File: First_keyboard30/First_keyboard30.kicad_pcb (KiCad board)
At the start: 2 copper layers, 238.1 x 57.2 mm, 0 parts

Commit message: circuit diagram compleat
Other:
- outline, holes or cut-outs redrawn

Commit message: pcb update
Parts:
- added D1: DIODE, kbd:D3_TH_SMD, F.Cu at (47.1, 93.0)
- added D10: DIODE, kbd:D3_TH_SMD, F.Cu at (218.6, 93.1)
- added D11: DIODE, kbd:D3_TH_SMD, F.Cu at (237.6, 93.1)
- added D12: DIODE, kbd:D3_TH_SMD, F.Cu at (261.4, 93.0)
- added D13: DIODE, kbd:D3_TH_SMD, F.Cu at (47.1, 110.7)
- added D14: DIODE, kbd:D3_TH_SMD, F.Cu at (66.2, 111.1)
- added D15: DIODE, kbd:D3_TH_SMD, F.Cu at (85.2, 111.0)
- added D16: DIODE, kbd:D3_TH_SMD, F.Cu at (104.2, 111.0)
- added D17: DIODE, kbd:D3_TH_SMD, F.Cu at (123.3, 111.0)
- added D18: DIODE, kbd:D3_TH_SMD, F.Cu at (142.4, 111.0)
- added D19: DIODE, kbd:D3_TH_SMD, F.Cu at (161.5, 110.3)
- added D2: DIODE, kbd:D3_TH_SMD, F.Cu at (66.2, 93.0)
- added D20: DIODE, kbd:D3_TH_SMD, F.Cu at (180.5, 110.4)
- added D21: DIODE, kbd:D3_TH_SMD, F.Cu at (199.5, 110.4)
- added D22: DIODE, kbd:D3_TH_SMD, F.Cu at (218.6, 110.3)
- added D23: DIODE, kbd:D3_TH_SMD, F.Cu at (237.5, 110.3)
- added D24: DIODE, kbd:D3_TH_SMD, F.Cu at (47.1, 129.3)
- added D25: DIODE, kbd:D3_TH_SMD, F.Cu at (66.2, 129.4)
- added D26: DIODE, kbd:D3_TH_SMD, F.Cu at (85.2, 129.4)
- added D27: DIODE, kbd:D3_TH_SMD, F.Cu at (104.2, 129.2)
- added D28: DIODE, kbd:D3_TH_SMD, F.Cu at (123.3, 129.2)
- added D29: DIODE, kbd:D3_TH_SMD, F.Cu at (142.3, 129.2)
- added D3: DIODE, kbd:D3_TH_SMD, F.Cu at (85.2, 93.0)
- added D30: DIODE, kbd:D3_TH_SMD, F.Cu at (243.4, 131.4)
- added D31: DIODE, kbd:D3_TH_SMD, F.Cu at (161.6, 129.3)
- added D32: DIODE, kbd:D3_TH_SMD, F.Cu at (180.5, 129.3)
- added D33: DIODE, kbd:D3_TH_SMD, F.Cu at (205.5, 129.3)
- added D34: DIODE, kbd:D3_TH_SMD, F.Cu at (243.4, 119.3)
- added D4: DIODE, kbd:D3_TH_SMD, F.Cu at (104.3, 92.9)
- added D5: DIODE, kbd:D3_TH_SMD, F.Cu at (123.3, 92.9)
- added D6: DIODE, kbd:D3_TH_SMD, F.Cu at (142.3, 93.0)
- added D7: DIODE, kbd:D3_TH_SMD, F.Cu at (161.5, 93.1)
- added D8: DIODE, kbd:D3_TH_SMD, F.Cu at (180.5, 93.1)
- added D9: DIODE, kbd:D3_TH_SMD, F.Cu at (199.5, 93.1)
- added SW1: RESET_SW, kbd:ResetSW, F.Cu at (32.9, 98.0)
- added SW10: KEY_SW, kbd:CherryMX_1u, F.Cu at (190.0, 92.5)
- added SW11: KEY_SW, kbd:CherryMX_1u, F.Cu at (209.0, 92.5)
- added SW12: KEY_SW, kbd:CherryMX_1u, F.Cu at (228.1, 92.5)
- added SW13: KEY_SW, kbd:CherryMX_1u, F.Cu at (251.9, 92.5)
- added SW14: KEY_SW, kbd:CherryMX_1u, F.Cu at (37.6, 111.6)
- added SW15: KEY_SW, kbd:CherryMX_1u, F.Cu at (56.6, 111.6)
- added SW16: KEY_SW, kbd:CherryMX_1u, F.Cu at (75.7, 111.6)
- added SW17: KEY_SW, kbd:CherryMX_1u, F.Cu at (94.7, 111.6)
- added SW18: KEY_SW, kbd:CherryMX_1u, F.Cu at (113.8, 111.6)
- added SW19: KEY_SW, kbd:CherryMX_1u, F.Cu at (132.8, 111.6)
- added SW2: KEY_SW, kbd:CherryMX_1u, F.Cu at (37.6, 92.5)
- added SW20: KEY_SW, kbd:CherryMX_1u, F.Cu at (151.9, 111.6)
- added SW21: KEY_SW, kbd:CherryMX_1u, F.Cu at (170.9, 111.6)
- added SW22: KEY_SW, kbd:CherryMX_1u, F.Cu at (190.0, 111.6)
- added SW23: KEY_SW, kbd:CherryMX_1u, F.Cu at (209.0, 111.6)
- added SW24: KEY_SW, kbd:CherryMX_1u, F.Cu at (228.1, 111.6)
- added SW25: KEY_SW, kbd:CherryMX_1u, F.Cu at (37.6, 130.6)
- added SW26: KEY_SW, kbd:CherryMX_1u, F.Cu at (56.6, 130.6)
- added SW27: KEY_SW, kbd:CherryMX_1u, F.Cu at (75.7, 130.6)
- added SW28: KEY_SW, kbd:CherryMX_1u, F.Cu at (94.7, 130.6)
- added SW29: KEY_SW, kbd:CherryMX_1u, F.Cu at (113.8, 130.6)
- added SW3: KEY_SW, kbd:CherryMX_1u, F.Cu at (56.6, 92.5)
- added SW30: KEY_SW, kbd:CherryMX_1u, F.Cu at (132.8, 130.6)
- added SW31: KEY_SW, Keebio-Parts:MX-Alps-Choc-2U, F.Cu at (224.4, 130.6)
- added SW32: KEY_SW, kbd:CherryMX_1u, F.Cu at (151.9, 130.6)
- added SW33: KEY_SW, kbd:CherryMX_1u, F.Cu at (170.9, 130.6)
- added SW34: KEY_SW, kbd:CherryMX_1u, F.Cu at (192.4, 130.6)
- added SW35: KEY_SW, Keebio-Parts:MX-Alps-Choc-2U, F.Cu at (254.2, 121.1)
- added SW4: KEY_SW, kbd:CherryMX_1u, F.Cu at (75.7, 92.5)
- added SW5: KEY_SW, kbd:CherryMX_1u, F.Cu at (94.7, 92.5)
- added SW6: KEY_SW, kbd:CherryMX_1u, F.Cu at (113.8, 92.5)
- added SW7: KEY_SW, kbd:CherryMX_1u, F.Cu at (132.8, 92.5)
- added SW8: KEY_SW, kbd:CherryMX_1u, F.Cu at (151.9, 92.5)
- added SW9: KEY_SW, kbd:CherryMX_1u, F.Cu at (170.9, 92.5)
- added U1: ProMicro, Keebio-Parts:ArduinoProMicro, F.Cu at (47.4, 110.1)

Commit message: update pcb
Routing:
- net col5: track 0.00 -> 308.4 mm, vias 0 -> 10
- net col3: track 0.00 -> 281.3 mm, vias 0 -> 4
- net col4: track 0.00 -> 245.6 mm, vias 0 -> 6
- net row1: track 0.00 -> 242.8 mm, vias 0 -> 4
- net col2: track 0.00 -> 222.4 mm, vias 0 -> 2
- net row3: track 0.00 -> 219.8 mm
- net col0: track 0.00 -> 214.1 mm
- net row4: track 0.00 -> 213.7 mm
- net row5: track 0.00 -> 204.3 mm
- net col1: track 0.00 -> 201.4 mm, vias 0 -> 2
- net row0: track 0.00 -> 141.6 mm
- net row2: track 0.00 -> 110.9 mm
- net Net-(D30-Pad1): track 0.00 -> 30.9 mm
- net GND: track 0.00 -> 28.2 mm
- net Net-(D34-Pad1): track 0.00 -> 12.6 mm
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
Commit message: GND mask
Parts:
- added REF**: MountingHole_2.2mm_M2, MountingHole:MountingHole_2.2mm_M2, F.Cu at (47.1, 137.8)
- added REF**: MountingHole_2.2mm_M2, MountingHole:MountingHole_2.2mm_M2, F.Cu at (47.1, 85.3)
- added REF**: MountingHole_2.2mm_M2, MountingHole:MountingHole_2.2mm_M2, F.Cu at (142.3, 85.4)
- added REF**: MountingHole_2.2mm_M2, MountingHole:MountingHole_2.2mm_M2, F.Cu at (245.6, 137.8)
- added REF**: MountingHole_2.2mm_M2, MountingHole:MountingHole_2.2mm_M2, F.Cu at (242.3, 85.3)
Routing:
- net Net-(D33-Pad1): track 0.00 -> 13.4 mm
- net Net-(D31-Pad1): track 0.00 -> 10.3 mm
- net Net-(D32-Pad1): track 0.00 -> 10.1 mm
- net Net-(D26-Pad1): track 0.00 -> 9.98 mm
- net Net-(D29-Pad1): track 0.00 -> 9.73 mm
- net Net-(D27-Pad1): track 0.00 -> 9.70 mm
- net Net-(D28-Pad1): track 0.00 -> 9.08 mm
- net row4: track 213.7 -> 222.3 mm
- net row1: track 242.8 -> 251.0 mm
- net row5: track 204.3 -> 210.4 mm
- net Net-(D30-Pad1): track 30.9 -> 32.9 mm
- net Net-(D16-Pad1): track 8.37 -> 10.4 mm
- added copper zone on B.Cu, net GND
- added copper zone on F.Cu, net GND

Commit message: draw dxf
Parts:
- moved REF** 0.19 mm to (245.4, 137.7)
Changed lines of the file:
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@@
       (padsonsilk false)
       (subtractmaskfromsilk false)
-      (outputformat 1)
+      (outputformat 3)
       (mirror false)
-      (drillshape 1)
+      (drillshape 0)
       (scaleselection 1)
-      (outputdirectory ""))
+      (outputdirectory "layout idea/"))
   )
   (net 0 "")
@@
   )
   (module MountingHole:MountingHole_2.2mm_M2 (layer F.Cu)
-    (at 245.56 137.76 90)
+    (at 245.38 137.71 90)
     (descr "Mounting Hole 2.2mm, no annular, M2")
     (tags "mounting hole 2.2mm no annular m2")

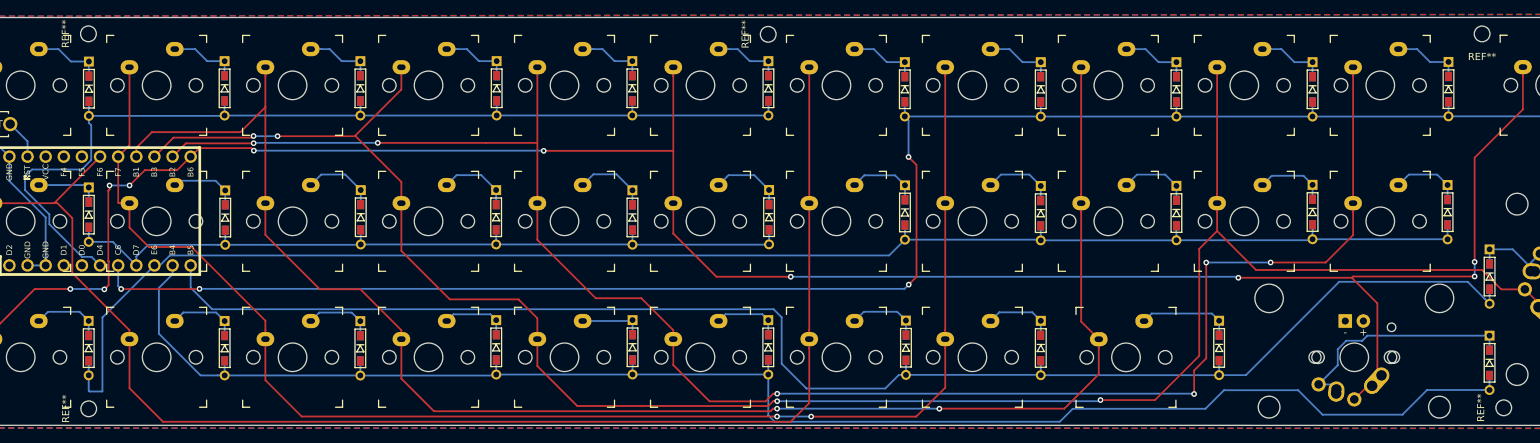
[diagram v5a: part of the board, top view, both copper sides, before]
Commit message: add logo
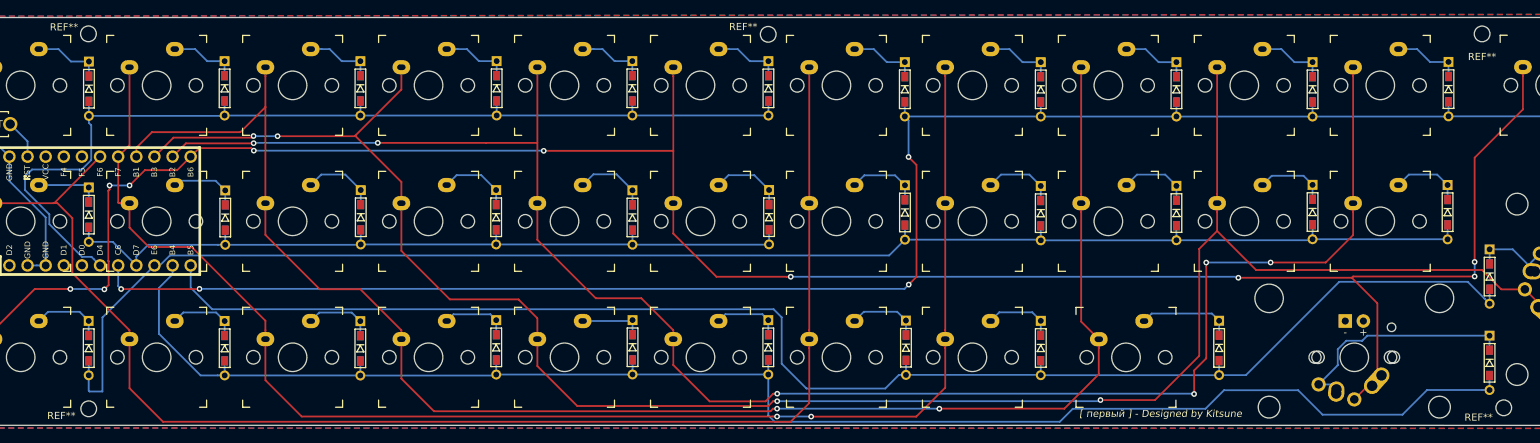
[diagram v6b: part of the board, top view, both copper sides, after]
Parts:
- added G***: LOGO, First_keyboard30:logo, B.Cu at (150.1, 110.1)
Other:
- board text added: "[ первый ] - Designed by Kitsune"

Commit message: rename
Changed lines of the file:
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@@
     (34 B.Paste user)
     (35 F.Paste user)
-    (36 B.SilkS user)
+    (36 B.SilkS user hide)
     (37 F.SilkS user)
     (38 B.Mask user)
@@
     (arrow2b (pts (xy 23.32523 83.021238) (xy 23.911946 84.147588)))
   )
-  (gr_text "[ первый ] - Designed by Kitsune" (at 197.31 138.53) (layer F.SilkS)
+  (gr_text "[ первый ] - Designed by Kitsune" (at 197.83 139.07) (layer F.SilkS)
     (effects (font (size 1 1) (thickness 0.15) italic))
   )

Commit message: fix pcb
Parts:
- turned D1 to 90 degrees
- turned D10 to 90 degrees
- turned D11 to 90 degrees
- turned D12 to 90 degrees
- turned D13 to 90 degrees
- turned D14 to 90 degrees
- turned D15 to 90 degrees
- turned D16 to 90 degrees
- turned D17 to 90 degrees
- turned D18 to 90 degrees
- turned D19 to 90 degrees
- turned D2 to 90 degrees
- turned D20 to 90 degrees
- turned D21 to 90 degrees
- turned D22 to 90 degrees
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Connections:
- D1 pad 1: Net-(D1-Pad1) -> row0
- D1 pad 2: row0 -> Net-(D1-Pad2)
- D10 pad 1: Net-(D10-Pad1) -> row1
- D10 pad 2: row1 -> Net-(D10-Pad2)
- D11 pad 1: Net-(D11-Pad1) -> row1
- D11 pad 2: row1 -> Net-(D11-Pad2)
- D12 pad 1: Net-(D12-Pad1) -> row1
- D12 pad 2: row1 -> Net-(D12-Pad2)
- D13 pad 1: Net-(D13-Pad1) -> row2
- D13 pad 2: row2 -> Net-(D13-Pad2)
- D14 pad 1: Net-(D14-Pad1) -> row2
- D14 pad 2: row2 -> Net-(D14-Pad2)
- D15 pad 1: Net-(D15-Pad1) -> row2
- D15 pad 2: row2 -> Net-(D15-Pad2)
- D16 pad 1: Net-(D16-Pad1) -> row2
- D16 pad 2: row2 -> Net-(D16-Pad2)
- D17 pad 1: Net-(D17-Pad1) -> row2
- D17 pad 2: row2 -> Net-(D17-Pad2)
- D18 pad 1: Net-(D18-Pad1) -> row2
- D18 pad 2: row2 -> Net-(D18-Pad2)
- D19 pad 1: Net-(D19-Pad1) -> row3
- D19 pad 2: row3 -> Net-(D19-Pad2)
- D2 pad 1: Net-(D2-Pad1) -> row0
- D2 pad 2: row0 -> Net-(D2-Pad2)
- D20 pad 1: Net-(D20-Pad1) -> row3
- D20 pad 2: row3 -> Net-(D20-Pad2)
- D21 pad 1: Net-(D21-Pad1) -> row3
- D21 pad 2: row3 -> Net-(D21-Pad2)
- D22 pad 1: Net-(D22-Pad1) -> row3
- D22 pad 2: row3 -> Net-(D22-Pad2)
- D23 pad 1: Net-(D23-Pad1) -> row3
- D23 pad 2: row3 -> Net-(D23-Pad2)
- D24 pad 1: Net-(D24-Pad1) -> row3
- D24 pad 2: row3 -> Net-(D24-Pad2)
- D25 pad 1: Net-(D25-Pad1) -> row4
- D25 pad 2: row4 -> Net-(D25-Pad2)
- D26 pad 1: Net-(D26-Pad1) -> row4
- D26 pad 2: row4 -> Net-(D26-Pad2)
- D27 pad 1: Net-(D27-Pad1) -> row4
- D27 pad 2: row4 -> Net-(D27-Pad2)
- D28 pad 1: Net-(D28-Pad1) -> row4
- D28 pad 2: row4 -> Net-(D28-Pad2)
- D29 pad 1: Net-(D29-Pad1) -> row4
- D29 pad 2: row4 -> Net-(D29-Pad2)
- D3 pad 1: Net-(D3-Pad1) -> row0
- D3 pad 2: row0 -> Net-(D3-Pad2)
- D30 pad 1: Net-(D30-Pad1) -> row4
- D30 pad 2: row4 -> Net-(D30-Pad2)
- D31 pad 1: Net-(D31-Pad1) -> row5
- D31 pad 2: row5 -> Net-(D31-Pad2)
- D32 pad 1: Net-(D32-Pad1) -> row5
- D32 pad 2: row5 -> Net-(D32-Pad2)
- D33 pad 1: Net-(D33-Pad1) -> row5
- D33 pad 2: row5 -> Net-(D33-Pad2)
- D34 pad 1: Net-(D34-Pad1) -> row5
- D34 pad 2: row5 -> Net-(D34-Pad2)
- D4 pad 1: Net-(D4-Pad1) -> row0
- D4 pad 2: row0 -> Net-(D4-Pad2)
- D5 pad 1: Net-(D5-Pad1) -> row0
- D5 pad 2: row0 -> Net-(D5-Pad2)
- D6 pad 1: Net-(D6-Pad1) -> row0
- D6 pad 2: row0 -> Net-(D6-Pad2)
- D7 pad 1: Net-(D7-Pad1) -> row1
- D7 pad 2: row1 -> Net-(D7-Pad2)
- D8 pad 1: Net-(D8-Pad1) -> row1
- D8 pad 2: row1 -> Net-(D8-Pad2)
- D9 pad 1: Net-(D9-Pad1) -> row1
- D9 pad 2: row1 -> Net-(D9-Pad2)
- SW10 pad 2: Net-(D9-Pad1) -> Net-(D9-Pad2)
- SW11 pad 2: Net-(D10-Pad1) -> Net-(D10-Pad2)
- SW12 pad 2: Net-(D11-Pad1) -> Net-(D11-Pad2)
- SW13 pad 2: Net-(D12-Pad1) -> Net-(D12-Pad2)
- SW14 pad 2: Net-(D13-Pad1) -> Net-(D13-Pad2)
- SW15 pad 2: Net-(D14-Pad1) -> Net-(D14-Pad2)
- SW16 pad 2: Net-(D15-Pad1) -> Net-(D15-Pad2)
- SW17 pad 2: Net-(D16-Pad1) -> Net-(D16-Pad2)
- SW18 pad 2: Net-(D17-Pad1) -> Net-(D17-Pad2)
- SW19 pad 2: Net-(D18-Pad1) -> Net-(D18-Pad2)
- SW2 pad 2: Net-(D1-Pad1) -> Net-(D1-Pad2)
- SW20 pad 2: Net-(D19-Pad1) -> Net-(D19-Pad2)
- SW21 pad 2: Net-(D20-Pad1) -> Net-(D20-Pad2)
- SW22 pad 2: Net-(D21-Pad1) -> Net-(D21-Pad2)
- SW23 pad 2: Net-(D22-Pad1) -> Net-(D22-Pad2)
- SW24 pad 2: Net-(D23-Pad1) -> Net-(D23-Pad2)
- SW25 pad 2: Net-(D24-Pad1) -> Net-(D24-Pad2)
- SW26 pad 2: Net-(D25-Pad1) -> Net-(D25-Pad2)
- SW27 pad 2: Net-(D26-Pad1) -> Net-(D26-Pad2)
- SW28 pad 2: Net-(D27-Pad1) -> Net-(D27-Pad2)
- SW29 pad 2: Net-(D28-Pad1) -> Net-(D28-Pad2)
- SW3 pad 2: Net-(D2-Pad1) -> Net-(D2-Pad2)
- SW30 pad 2: Net-(D29-Pad1) -> Net-(D29-Pad2)
- SW31 pad 2: Net-(D30-Pad1) -> Net-(D30-Pad2)
- SW32 pad 2: Net-(D31-Pad1) -> Net-(D31-Pad2)
- SW33 pad 2: Net-(D32-Pad1) -> Net-(D32-Pad2)
- SW34 pad 2: Net-(D33-Pad1) -> Net-(D33-Pad2)
- SW35 pad 2: Net-(D34-Pad1) -> Net-(D34-Pad2)
- SW4 pad 2: Net-(D3-Pad1) -> Net-(D3-Pad2)
- SW5 pad 2: Net-(D4-Pad1) -> Net-(D4-Pad2)
- SW6 pad 2: Net-(D5-Pad1) -> Net-(D5-Pad2)
- SW7 pad 2: Net-(D6-Pad1) -> Net-(D6-Pad2)
- SW8 pad 2: Net-(D7-Pad1) -> Net-(D7-Pad2)
- SW9 pad 2: Net-(D8-Pad1) -> Net-(D8-Pad2)
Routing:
- net Net-(D30-Pad2): track 0.00 -> 32.9 mm
- net Net-(D30-Pad1): track 32.9 -> 0.00 mm
- net Net-(D33-Pad2): track 0.00 -> 13.4 mm
- net Net-(D33-Pad1): track 13.4 -> 0.00 mm
- net Net-(D34-Pad2): track 0.00 -> 12.6 mm
- net Net-(D34-Pad1): track 12.6 -> 0.00 mm
- net Net-(D17-Pad2): track 0.00 -> 10.6 mm
- net Net-(D17-Pad1): track 10.6 -> 0.00 mm
- net Net-(D15-Pad2): track 0.00 -> 10.6 mm
- net Net-(D15-Pad1): track 10.6 -> 0.00 mm
- net Net-(D18-Pad2): track 0.00 -> 10.5 mm
- net Net-(D18-Pad1): track 10.5 -> 0.00 mm
- net Net-(D16-Pad2): track 0.00 -> 10.4 mm
- net Net-(D16-Pad1): track 10.4 -> 0.00 mm
- net Net-(D20-Pad2): track 0.00 -> 10.3 mm
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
